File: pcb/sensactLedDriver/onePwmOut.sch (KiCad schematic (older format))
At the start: 10 parts, among them P22 CONN_01X02, U17 LM3404

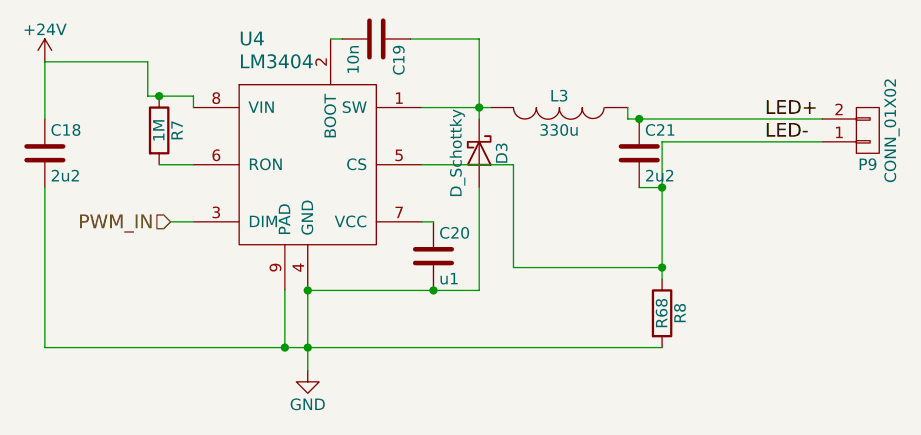
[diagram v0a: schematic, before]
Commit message: Every application knows its apptype
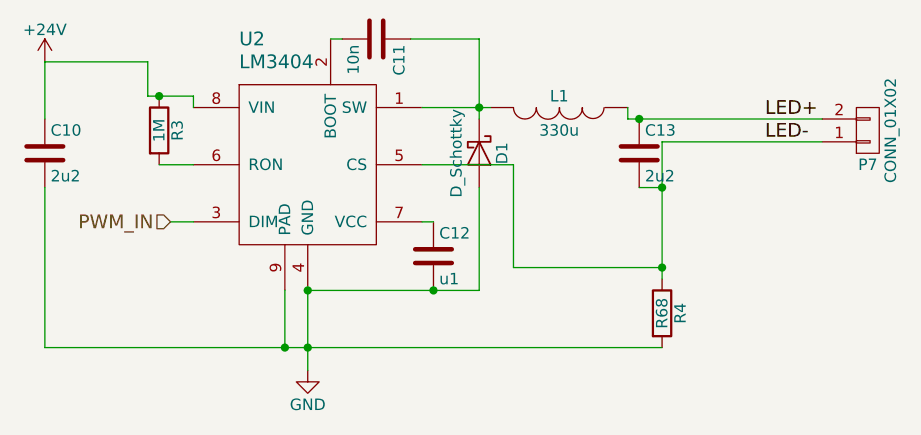
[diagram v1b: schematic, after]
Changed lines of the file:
@@
 AR Path="/57CDCE6B/57CCF041" Ref="P20"  Part="1"
 AR Path="/57CDCE97/57CCF041" Ref="P21"  Part="1"
-F 0 "P9" H 8200 3550 50  0000 C CNN
+F 0 "P7" H 8200 3550 50  0000 C CNN
 F 1 "CONN_01X02" V 8300 3400 50  0000 C CNN
 F 2 "sensact:conn_2P" H 8200 3400 50  0001 C CNN
@@
 P 5750 4450
 AR Path="/57CDCEC1/57CCF171" Ref="#PWR049"  Part="1"
-AR Path="/57CCF017/57CCF171" Ref="#PWR024"  Part="1"
-AR Path="/57CD0726/57CCF171" Ref="#PWR026"  Part="1"
-AR Path="/57CD07F6/57CCF171" Ref="#PWR028"  Part="1"
-AR Path="/57CD080D/57CCF171" Ref="#PWR030"  Part="1"
+AR Path="/57CCF017/57CCF171" Ref="#PWR022"  Part="1"
+AR Path="/57CD0726/57CCF171" Ref="#PWR024"  Part="1"
+AR Path="/57CD07F6/57CCF171" Ref="#PWR026"  Part="1"
+AR Path="/57CD080D/57CCF171" Ref="#PWR028"  Part="1"
 AR Path="/57CD0824/57CCF171" Ref="#PWR032"  Part="1"
 AR Path="/57CD083B/57CCF171" Ref="#PWR034"  Part="1"
@@
 P 4600 3100
 AR Path="/57CDCEC1/57CCF189" Ref="#PWR050"  Part="1"
-AR Path="/57CCF017/57CCF189" Ref="#PWR025"  Part="1"
-AR Path="/57CD0726/57CCF189" Ref="#PWR027"  Part="1"
-AR Path="/57CD07F6/57CCF189" Ref="#PWR029"  Part="1"
-AR Path="/57CD080D/57CCF189" Ref="#PWR031"  Part="1"
+AR Path="/57CCF017/57CCF189" Ref="#PWR023"  Part="1"
+AR Path="/57CD0726/57CCF189" Ref="#PWR025"  Part="1"
+AR Path="/57CD07F6/57CCF189" Ref="#PWR027"  Part="1"
+AR Path="/57CD080D/57CCF189" Ref="#PWR029"  Part="1"
 AR Path="/57CD0824/57CCF189" Ref="#PWR033"  Part="1"
 AR Path="/57CD083B/57CCF189" Ref="#PWR035"  Part="1"
@@
 AR Path="/57CDCE6B/58432375" Ref="U15"  Part="1"
 AR Path="/57CDCE97/58432375" Ref="U16"  Part="1"
-F 0 "U4" H 5450 4400 60  0000 L CNN
+F 0 "U2" H 5450 4400 60  0000 L CNN
 F 1 "LM3404" H 5450 4300 60  0000 L CNN
 F 2 "sensact:SOIC-8_3.9x4.9mm_Pitch1.27mm_pad_handsolder" H 5800 3700 60  0001 C CNN
@@
 AR Path="/57CDCE6B/584323DE" Ref="R29"  Part="1"
 AR Path="/57CDCE97/584323DE" Ref="R31"  Part="1"
-F 0 "R7" V 5180 3400 50  0000 C CNN
+F 0 "R3" V 5180 3400 50  0000 C CNN
 F 1 "1M" V 5100 3400 50  0000 C CNN
 F 2 "Resistors_SMD:R_0805_HandSoldering" V 5030 3400 50  0001 C CNN
@@
 AR Path="/57CDCE6B/5843248F" Ref="D14"  Part="1"
 AR Path="/57CDCE97/5843248F" Ref="D15"  Part="1"
-F 0 "D3" H 6500 3600 50  0000 C CNN
+F 0 "D1" H 6500 3600 50  0000 C CNN
 F 1 "D_Schottky" H 6500 3400 50  0000 C CNN
 F 2 "sensact:do214ac_handsolder" H 6500 3500 50  0001 C CNN
@@
 AR Path="/57CDCE6B/584324F2" Ref="L14"  Part="1"
 AR Path="/57CDCE97/584324F2" Ref="L15"  Part="1"
-F 0 "L3" V 6800 3300 50  0000 C CNN
+F 0 "L1" V 6800 3300 50  0000 C CNN
 F 1 "330u" V 6950 3300 50  0000 C CNN
 F 2 "sensact:CD127" H 6850 3300 50  0001 C CNN
@@
 AR Path="/57CDCE6B/584326A5" Ref="R30"  Part="1"
 AR Path="/57CDCE97/584326A5" Ref="R32"  Part="1"
-F 0 "R8" V 7380 4200 50  0000 C CNN
+F 0 "R4" V 7380 4200 50  0000 C CNN
 F 1 "R68" V 7300 4200 50  0000 C CNN
 F 2 "Resistors_SMD:R_2512_HandSoldering" V 7230 4200 50  0001 C CNN
@@
 AR Path="/57CDCE6B/58432966" Ref="C64"  Part="1"
 AR Path="/57CDCE97/58432966" Ref="C68"  Part="1"
-F 0 "C20" H 6325 4050 50  0000 L CNN
+F 0 "C12" H 6325 4050 50  0000 L CNN
 F 1 "u1" H 6325 3850 50  0000 L CNN
 F 2 "Resistors_SMD:R_0805_HandSoldering" H 6338 3800 50  0001 C CNN
@@
 AR Path="/57CDCE6B/58432A2E" Ref="C62"  Part="1"
 AR Path="/57CDCE97/58432A2E" Ref="C66"  Part="1"
-F 0 "C18" H 4625 3600 50  0000 L CNN
+F 0 "C10" H 4625 3600 50  0000 L CNN
 F 1 "2u2" H 4625 3400 50  0000 L CNN
 F 2 "Resistors_SMD:R_1210_HandSoldering" H 4638 3350 50  0001 C CNN
@@
 AR Path="/57CDCE6B/58432B9C" Ref="C65"  Part="1"
 AR Path="/57CDCE97/58432B9C" Ref="C69"  Part="1"
-F 0 "C21" H 7225 3600 50  0000 L CNN
+F 0 "C13" H 7225 3600 50  0000 L CNN
 F 1 "2u2" H 7225 3400 50  0000 L CNN
 F 2 "Resistors_SMD:R_1210_HandSoldering" H 7238 3350 50  0001 C CNN
@@
 AR Path="/57CDCE6B/58432D09" Ref="C63"  Part="1"
 AR Path="/57CDCE97/58432D09" Ref="C67"  Part="1"
-F 0 "C19" H 6075 3100 50  0000 L CNN
+F 0 "C11" H 6075 3100 50  0000 L CNN
 F 1 "10n" H 6075 2900 50  0000 L CNN
 F 2 "Resistors_SMD:R_0805_HandSoldering" H 6088 2850 50  0001 C CNN
